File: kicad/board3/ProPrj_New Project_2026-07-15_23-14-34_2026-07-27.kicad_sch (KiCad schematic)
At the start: 143 parts, among them P1 WJ500V-5.08-2P, P2 WJ500V-5.08-2P, Q1 AO4406A, Q2 AO4406A, SW1 HX TS4538CJ 250gf 009, SW2 HX TS4538CJ 250gf 009, SW3 HX TS4538CJ 250gf 009, SW4 HX TS4538CJ 250gf 009, SW6 HX TS4538CJ 250gf 009, SW7 HX TS4538CJ 250gf 009, U1 STM32H755ZIT6, U11 AW9523BTQR, U12 AW9523BTQR, U2 W25Q256JVEIQ, U3 TPS563201DDCR, U4 CH224K, U5 LM74700QDBVRQ1, U6 LM74700QDBVRQ1, U7 FM24CL64B-GTR, U8 TJA1051T/3/1J, U9 TJA1051T/3/1J, X1 25MHz

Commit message: fix(kicad): U35 -- merge two duplicate part numbers, 48 BOM lines to 46
Two pairs were electrically identical and same-package, differing only in
manufacturer, and in each case one side was Basic while the other was Extended:

  C17-C28              C1591  Samsung   -> C14663 YAGEO      100nF 50V X7R 0603
  R11-R13, R45-R47     C98220 YAGEO     -> C25804 UNI-ROYAL  10k 1% 100mW 0603

They existed as separate lines only because the parts arrived in different
EasyEDA import batches -- both are contiguous refdes blocks.

Every identity value was COPIED from an instance already carrying the target
part (C6 and R1) rather than hand-typed. Retyping a part's fields is how this
project produced a 3 nm footprint mismatch that survived an entire campaign;
one source of truth avoids it. The script aborts if any target does not carry
the expected old code.

Found while doing it: the six C98220 resistors were already using the
UNI-ROYAL symbol (0603WAF1002T5E) while carrying YAGEO properties, so the
symbol and the metadata disagreed before this change. The merge settles that
too.

Verified gerber-neutral, which was the point of doing it this way -- all six
layers diff to ZERO lines once the CreationDate header is excluded. "Byte
identical" is not achievable as a criterion because gerbers embed a generation
timestamp; identical-ignoring-CreationDate is the real test. CPL byte-identical.
No GUI sync needed: Value strings were already identical on both sides, so the
board footprints' Value fields were already correct (the U10/U24 precedent).

Also removes fab/board3-gerbers.zip (U40) -- a degraded-run decoy whose board
outline was named Multi-Layer, which to a fab means the opposite of an outline.

Co-Authored-By: Claude Opus 5 (1M context) <noreply@anthropic.com>
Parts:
- C17, C18, C19, C20, C21, C22, C23, C24, C25, C26, C27, C28: symbol ProPrj_New-easyedapro:CL10B104KB8NNNC -> ProPrj_New-easyedapro:CC0603KRX7R9BB104; JLCPCB Part Class Extended Part -> Basic Part; Manufacturer SAMSUNG(三星) -> YAGEO(国巨); Manufacturer Part CL10B104KB8NNNC -> CC0603KRX7R9BB104; Supplier Part C1591 -> C14663
- R11, R12, R13, R45, R46, R47: Manufacturer YAGEO -> UNI-ROYAL(厚声); Manufacturer Part RC0603FR-0710KL -> 0603WAF1002T5E; Supplier Part C98220 -> C25804

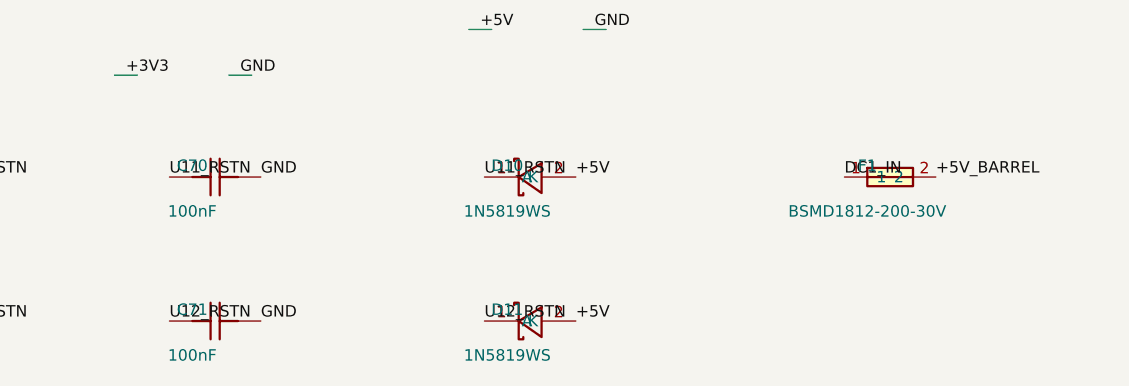
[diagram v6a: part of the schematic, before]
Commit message: fix(kicad): U32 F1 to a 3 A PTC, U34 RSTN caps to 1 uF
U32 -- F1 was C960026, 2 A hold, derating to ~1.4 A at 60 C against an input
path this project's own layout guide rates at 1.5-2 A. Two independent load
tallies during review came out at 1.74 A and 1.90 A. The previous plan's stop
condition ("above ~1.3 A the part moves up a size before order") was already
satisfied by numbers sitting in the repo -- no bench measurement was ever
needed to fire it. A latched PPTC means the dash goes dark mid-session and
stays dark until DC1 is unplugged and the part cools.

Now C48985875: 3 A hold / 5 A trip, 30 V, 47.5 k stock, and 10 mOhm initial
resistance against the old part's 20 -- which also halves its contribution to
the input-path voltage drop U33 exists to fix. Same 1812 land, verified pad for
pad: identical positions, sizes and shapes, so existing copper lands unchanged.

U34 -- C70/C71 at 100 nF only meet the ~100 us RSTN hold for rail ramps faster
than about 4 ms, and the ramp here is set by the adapter, the LM74700 gate slew
and ~76 uF of bulk. Nobody has measured it. 1 uF covers ramps to 50 ms.

U34 turned out to need NO new part: C15849 (1 uF 50 V X5R 0603) was already on
this board at C40/C47/C50. C70/C71 now carry C40's identity exactly, so they
merge into that existing line rather than starting a new one -- BOM stays at 46
and the footprint does not change, so U34 needs no sync at all. The 50 V rating
on a 5 V rail keeps DC-bias derating small, which matters for a timing cap.

Two things went wrong on the way and are worth recording.

First, editing an instance's lib_id to a symbol that is not in the schematic's
embedded (lib_symbols) cache does not raise anything -- the part simply
DISAPPEARS FROM THE BOM while still appearing in the CPL. bom_cpl_symmetry()
caught it and named the parts: "in CPL, absent from BOM (3): C70, C71, F1".
That gate was written three commits ago for exactly this class and has now paid
for itself. lib_id is left pointing at the origina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
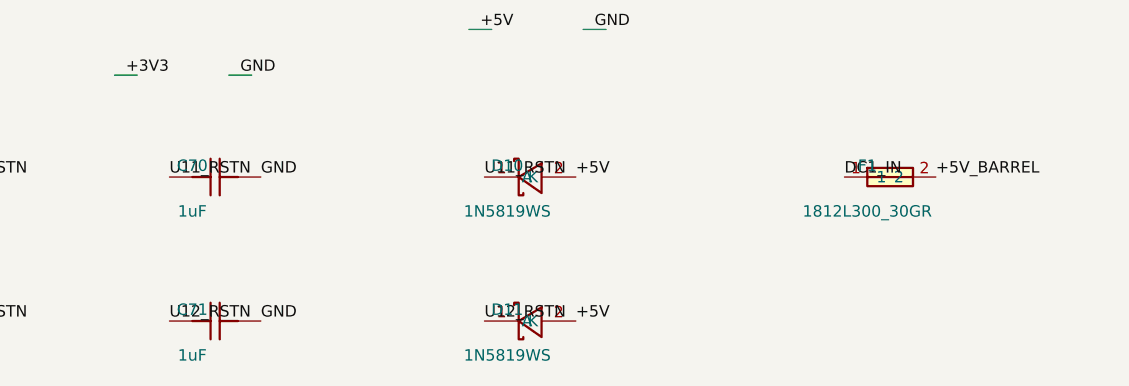
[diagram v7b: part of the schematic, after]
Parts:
- C70, C71: value 100nF -> 1uF; Manufacturer YAGEO -> SAMSUNG(三星); Manufacturer Part CC0603KRX7R9BB104 -> CL10A105KB8NNNC; Supplier Part C14663 -> C15849
- F1: value BSMD1812-200-30V -> 1812L300_30GR; footprint JLCImport:BSMD1812-200-30V -> JLCImport:1812L300_30GR; Manufacturer BHFUSE -> LUTE; Manufacturer Part BSMD1812-200-30V -> 1812L300/30GR; Supplier Part C960026 -> C48985875
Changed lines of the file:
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@@
 			)
 		)
-		(property "Value" "100nF"
+		(property "Value" "1uF"
 			(at 92.46 375.81 0)
 			(effects
@@
 			)
 		)
-		(property "Datasheet" ""
-			(at 95.0 372.0 0)
-			(hide yes)
-			(effects
-				(font
-					(size 1.27 1.27)
-				)
-			)
-		)
-		(property "Description" "100nF 50V X7R 0603"
-			(at 95.0 372.0 0)
-			(hide yes)
-			(effects
-				(font
-					(size 1.27 1.27)
-				)
-			)
-		)
-		(property "Manufacturer Part" "CC0603KRX7R9BB104"
-			(at 95.0 372.0 0)
-			(hide yes)
-			(effects
-				(font
-					(size 1.27 1.27)
-				)
-			)
-		)
-		(property "Manufacturer" "YAGEO"
-			(at 95.0 372.0 0)
-			(hide yes)
-			(effects
-				(font
-					(size 1.27 1.27)
-				)
-			)
-		)
-		(property "Supplier Part" "C14663"
+		(property "Datasheet" "https://item.szlcsc.com/datasheet/CL10A105KB8NNNC/16531.html"
+			(at 95.0 372.0 0)
+			(hide yes)
+			(effects
+				(font
+					(size 1.27 1.27)
+				)
+			)
+		)
+		(property "Description" "Capacitance:1uF Tolerance:±10% Tolerance:±10% Voltage Rating:50V Temperature Coefficient:X5R"
+			(at 95.0 372.0 0)
+			(hide yes)
+			(effects
+				(font
+					(size 1.27 1.27)
+				)
+			)
+		)
+		(property "Manufacturer Part" "CL10A105KB8NNNC"
+			(at 95.0 372.0 0)
+			(hide yes)
+			(effects
+				(font
+					(size 1.27 1.27)
+				)
+			)
+		)
+		(property "Manufacturer" "SAMSUNG(三星)"
+			(at 95.0 372.0 0)
+			(hide yes)
+			(effects
+				(font
+					(size 1.27 1.27)
+				)
+			)
+		)
+		(property "Supplier Part" "C15849"
 			(at 95.0 372.0 0)
 			(hide yes)
@@
 			)
 		)
-		(property "Value" "100nF"
+		(property "Value" "1uF"
 			(at 92.46 391.81 0)
 			(effects
@@
 			)
 		)
-		(property "Datasheet" ""
-			(at 95.0 388.0 0)
-			(hide yes)
-			(effects
-				(font
-					(size 1.27 1.27)
-				)
-			)
-		)
-		(property "Description" "100nF 50V X7R 0603"
-			(at 95.0 388.0 0)
-			(hide yes)
-			(effects
-				(font
-					(size 1.27 1.27)
-				)
-			)
-		)
-		(property "Manufacturer Part" "CC0603KRX7R9BB104"
-			(at 95.0 388.0 0)
-			(hide yes)
-			(effects
-				(font
-					(size 1.27 1.27)
-				)
-			)
-		)
-		(property "Manufacturer" "YAGEO"
-			(at 95.0 388.0 0)
-			(hide yes)
-			(effects
-				(font
-					(size 1.27 1.27)
-				)
-			)
-		)
-		(property "Supplier Part" "C14663"
+		(property "Datasheet" "https://item.szlcsc.com/datasheet/CL10A105KB8NNNC/16531.html"
+			(at 95.0 388.0 0)
+			(hide yes)
+			(effects
+				(font
+					(size 1.27 1.27)
+				)
+			)
+		)
+		(property "Description" "Capacitance:1uF Tolerance:±10% Tolerance:±10% Voltage Rating:50V Temperature Coefficient:X5R"
+			(at 95.0 388.0 0)
+			(hide yes)
+			(effects
+				(font
+					(size 1.27 1.27)
+				)
+			)
+		)
+		(property "Manufacturer Part" "CL10A105KB8NNNC"
+			(at 95.0 388.0 0)
+			(hide yes)
+			(effects
+				(font
+					(size 1.27 1.27)
+				)
+			)
+		)
+		(property "Manufacturer" "SAMSUNG(三星)"
+			(at 95.0 388.0 0)
+			(hide yes)
+			(effects
+				(font
+					(size 1.27 1.27)
+				)
+			)
+		)
+		(property "Supplier Part" "C15849"
 			(at 95.0 388.0 0)
 			(hide yes)
@@
 			)
 		)
-		(property "Value" "BSMD1812-200-30V"
+		(property "Value" "1812L300_30GR"
 			(at 167.46 375.81 0)
 			(effects
@@
 			)
 		)
-		(property "Footprint" "JLCImport:BSMD1812-200-30V"
+		(property "Footprint" "JLCImport:1812L300_30GR"
 			(at 170.0 372.0 0)
 			(hide yes)
@@
 			)
 		)
-		(property "Datasheet" "https://www.lcsc.com/product-detail/C960026.html"
+		(property "Datasheet" "https://item.szlcsc.com/343302.html"
 			(at 170.0 372.0 0)
 			(hide yes)
@@
 			)
 		)
-		(property "Description" "PPTC 2A hold 4A trip 30V 1812"
+		(property "Description" "1812L300/30GR; F1812; LUTE"
 			(at 170.0 372.0 0)
 			(hide yes)
@@
 			)
 		)
-		(property "Manufacturer Part" "BSMD1812-200-30V"
+		(property "Manufacturer Part" "1812L300/30GR"
 			(at 170.0 372.0 0)
 			(hide yes)
@@
 			)
 		)
-		(property "Manufacturer" "BHFUSE"
+		(property "Manufacturer" "LUTE"
 			(at 170.0 372.0 0)
 			(hide yes)
@@
 			)
 		)
-		(property "Supplier Part" "C960026"
+		(property "Supplier Part" "C48985875"
 			(at 170.0 372.0 0)
 			(hide yes)

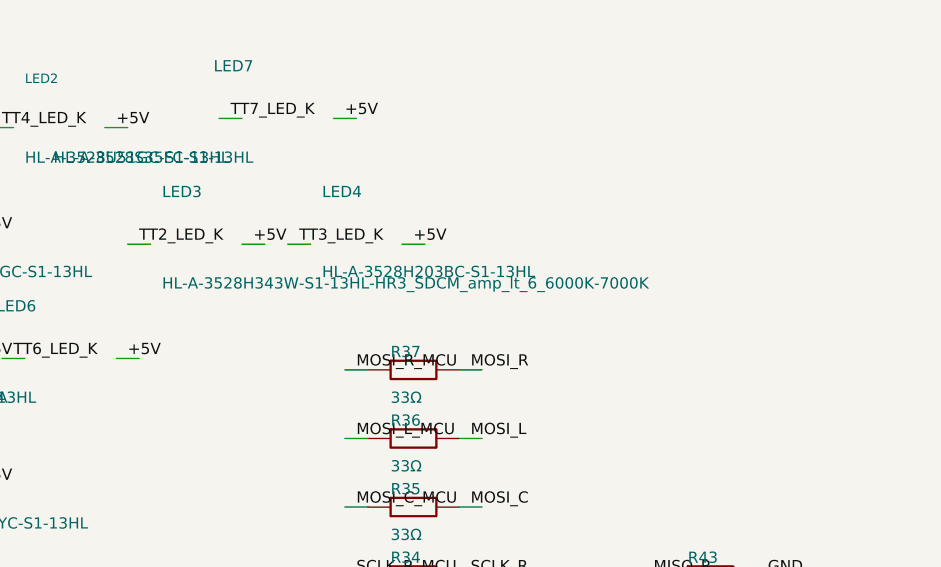
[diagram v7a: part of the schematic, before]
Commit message: fix(kicad): U46 -- complete the Part Class column and de-mangle LED3's MPN
Part Class is Basic vs Extended, which drives assembly cost: Extended parts
carry a per-reel feeder fee. It is absent from bom-jlcpcb.csv so it was never an
upload risk -- but it is the column a human quotes from, and 11 of 46 lines were
blank, including every part this campaign touched (D10/D11, F1, U2). A budget
built from that file understated the fee count.

Now complete: 18 Basic, 28 Extended, zero blank. Those 28 extended lines are
roughly $84 of feeder setup at $3 each, which independently matches the review's
~$87 estimate -- so the number is now visible in the file rather than only in a
reviewer's notes.

Class came from a SIBLING instance carrying the same Supplier Part wherever one
existed, keeping the board its own source of truth; 35 codes resolved that way.
Only codes with no annotated sibling used a map, and every one of those was read
from live JLC data this session rather than inferred from the part looking cheap
or common.

Took two passes, and the first one lied. It only REPLACED the property where it
already existed and silently no-opped where it did not -- while still
incrementing the counter, so it reported "filled 19" against a BOM that still
showed 11 blanks. 34 instances carried no such property at all. The fix adds the
property block; the lesson is that a counter incremented before the write is
confirmed is not evidence, and the BOM re-export is.

LED3's value also carried HTML-escape damage that survived the EasyEDA import:
"..._SDCM_amp_lt_6_6000K-7000K" is a mangled "&lt;". Now reads
HL-A-3528H343W-S1-13HL-HR3(SDCM 6)(6000K-7000K), matching LCSC's own model
string. Cosmetic for ordering -- the LCSC code picks the part -- but that string
is what the Component Marking Layer carries. The footprint NAME keeps the
mangled form: renaming it touches the library file, the board instance and every
reference, which is real risk for no fabrication benefit, since the marking
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
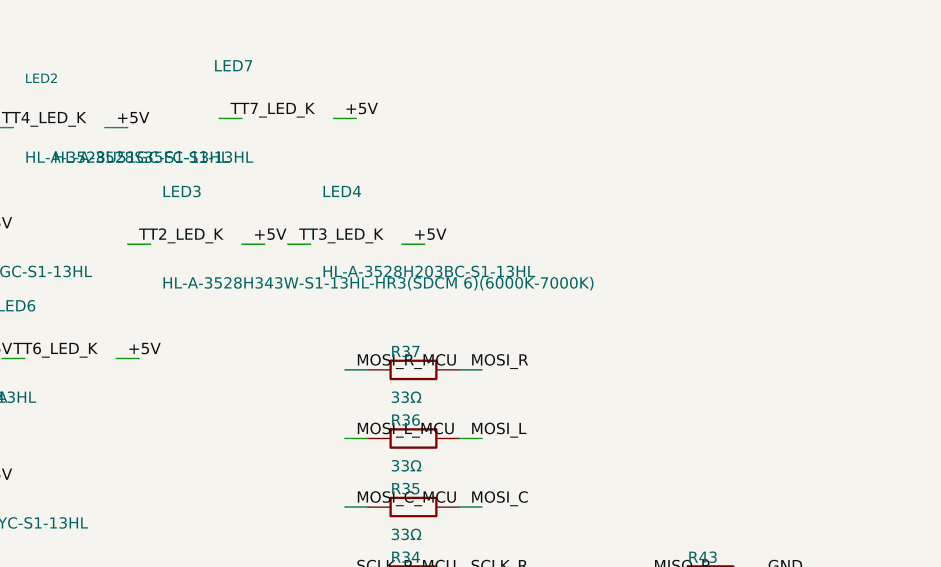
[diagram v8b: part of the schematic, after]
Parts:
- C10, C11, C15, C3, C32, C33, C34, C36, C38, C39, C4, C40, C5, C7, C70, C71, C8, C9, D10, D11, L1, R60, R61, X1: JLCPCB Part Class (none) -> Basic Part
- F1, SW1, SW2, SW3, SW4, SW6, SW7, U1, U2, U3: JLCPCB Part Class (none) -> Extended Part
- LED3: value HL-A-3528H343W-S1-13HL-HR3_SDCM_amp_lt_6_6000K-7000K -> HL-A-3528H343W-S1-13HL-HR3(SDCM 6)(6000K-7000K); Manufacturer Part HL-A-3528H343W-S1-13HL-HR3_SDCM_amp_lt_6_6000K-7000K -> HL-A-3528H343W-S1-13HL-HR3(SDCM 6)(6000K-7000K)
